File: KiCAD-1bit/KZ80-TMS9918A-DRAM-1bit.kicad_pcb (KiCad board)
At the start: 2 copper layers, 100 x 75 mm, 48 parts, among them J2 EXT_JP, J3 SBC8080 BUS, J4 AD_JP, J5 AD_JP, Q1 2SC1815, U1 TMS9918A, U10 MB8118-16k-1bit-DRAM, U11 MB8118-16k-1bit-DRAM, U12 MB8118-16k-1bit-DRAM, U2 74HCT32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

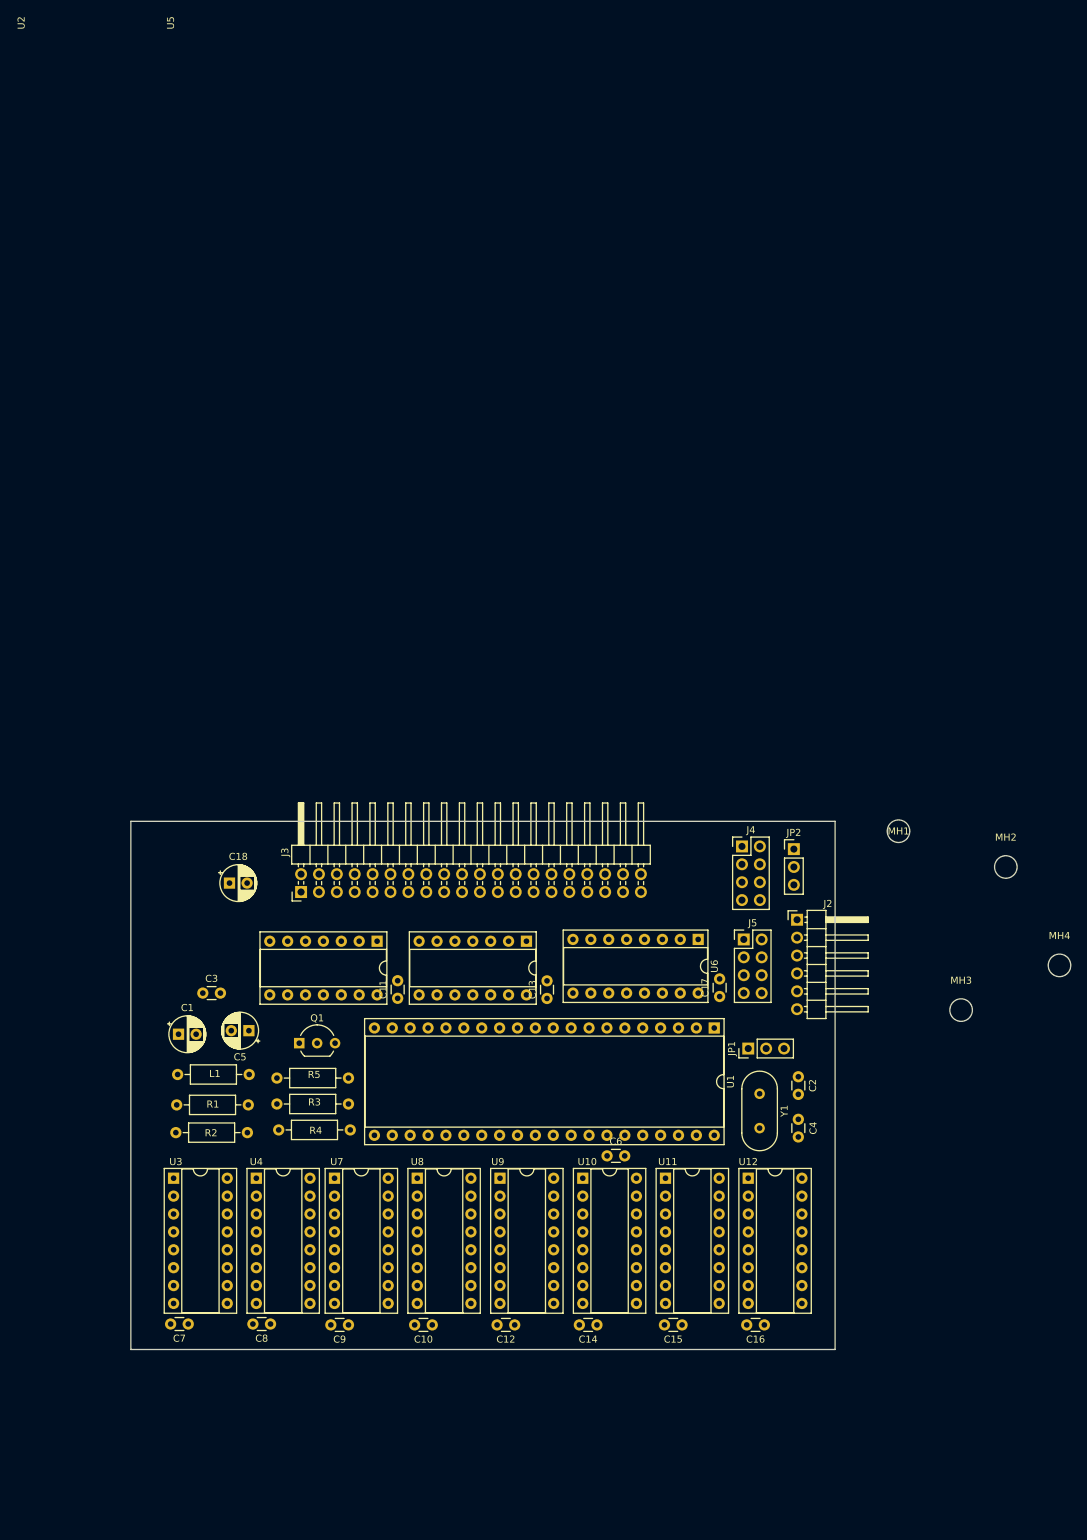
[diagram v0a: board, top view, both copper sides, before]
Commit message: DRAM 16kx1bit版プリントパターン作成
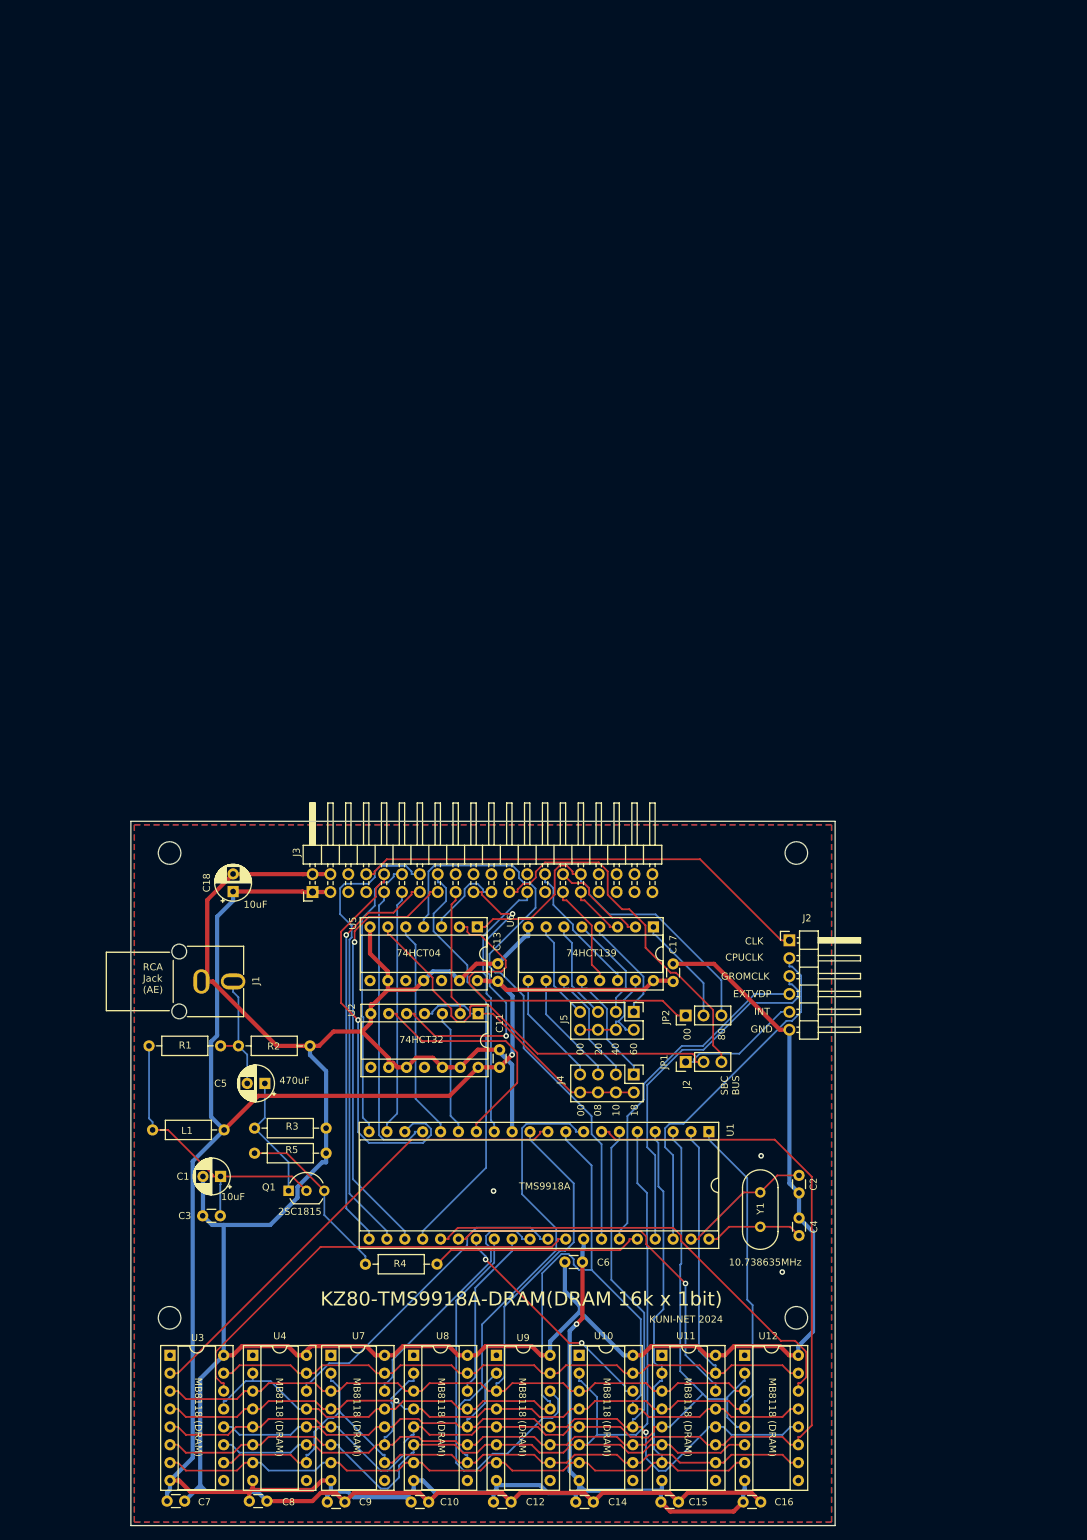
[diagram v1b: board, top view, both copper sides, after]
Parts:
- added J1: Conn_Coaxial, RCA:RCAConAE, F.Cu at (76.0, 78.7)
- moved MH3 120.6 mm to (71.5, 126.5)
- moved MH1 103.6 mm to (71.5, 60.5)
- moved MH4 62.5 mm to (160.5, 126.5)
- moved J4 35.8 mm to (137.4, 91.9), turned to -90 degrees
- moved C3 31.7 mm to (78.7, 112.0), turned to 180 degrees
- moved MH2 29.8 mm to (160.5, 60.5)
- moved R4 29.5 mm to (109.5, 118.9), turned to 180 degrees
- moved JP2 28.2 mm to (144.8, 83.6), turned to 90 degrees
- moved C10 25.2 mm to (108.3, 152.7)
- moved C14 25.2 mm to (131.7, 152.7)
- moved C12 25.2 mm to (120.0, 152.7)
- moved C15 25.2 mm to (143.8, 152.7)
- moved C16 25.2 mm to (155.4, 152.7)
- moved C9 25.2 mm to (96.4, 152.7)
- moved C7 25.2 mm to (73.6, 152.5)
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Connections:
- net Net-(U1-R/~{W}) renamed /R~{W}
- U1 pad 6: /AD1 -> /AD4
- U10 pad 12: /AD1 -> /AD4
- U11 pad 12: /AD1 -> /AD4
- U12 pad 12: /AD1 -> /AD4
- U3 pad 12: unconnected-(U3-A3-Pad12) -> /AD4
- U4 pad 12: /AD1 -> /AD4
- U7 pad 12: /AD1 -> /AD4
- U8 pad 12: /AD1 -> /AD4
- U9 pad 12: /AD1 -> /AD4
- U9 pad 2: /AD1 -> /AD4
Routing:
- net GND: track 0.00 -> 484.4 mm, vias 0 -> 3
- net VCC: track 0.00 -> 333.1 mm, vias 0 -> 2
- net /AD3: track 0.00 -> 172.4 mm
- net /AD2: track 0.00 -> 167.9 mm
- net /AD5: track 0.00 -> 157.1 mm
- net /AD1: track 0.00 -> 153.4 mm
- net /AD4: track 0.00 -> 149.4 mm, vias 0 -> 1
- net /AD7: track 0.00 -> 143.3 mm
- net /AD6: track 0.00 -> 138.3 mm
- net /R~{W}: track 0.00 -> 132.7 mm
- net /~{RAS}: track 0.00 -> 130.7 mm, vias 0 -> 1
- net /~{CAS}: track 0.00 -> 124.0 mm
- net /~{RES}: track 0.00 -> 85.0 mm
- net /AD0: track 0.00 -> 68.0 mm
- net /VD7: track 0.00 -> 66.7 mm
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- added copper zone on B.Cu, net GND
- added copper zone on F.Cu, net GND
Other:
- board size 100 x 75 mm -> 100 x 100 mm
- board text added: "00"
- board text added: "08"
- board text added: "10"
- board text added: "10.738635MHz"
- board text added: "10uF"
- board text added: "18"
- board text added: "20"
- board text added: "2SC1815"
- board text added: "40"
- board text added: "470uF"
- board text added: "60"
- board text added: "74HCT04"
- board text added: "74HCT139"
- board text added: "74HCT32"
- board text added: "80"
- board text added: "CLK"
- board text added: "CPUCLK"
- board text added: "EXTVDP"
- board text added: "GND"
- board text added: "GROMCLK"
- board text added: "INT"
- board text added: "J2"
- board text added: "KUNI-NET 2024"
- board text added: "KZ80-TMS9918A-DRAM(DRAM 16k x 1bit)"
- board text added: "MB8118 (DRAM)"
- board text added: "RCA Jack (AE)"
- board text added: "SBC BUS"
- board text added: "TMS9918A"

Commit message: シルク印刷間違い修正(64bit、16kbit両方) REV1.1ガーバー出力
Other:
- board text added: "REV.1.1"
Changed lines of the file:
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@@
     (aux_axis_origin 66 156)
     (pcbplotparams
-      (layerselection 0x00010fc_ffffffff)
+      (layerselection 0x00010f0_ffffffff)
       (plot_on_all_layers_selection 0x0000000_00000000)
       (disableapertmacros false)
@@
   (gr_rect (start 66 56) (end 166 156)
     (stroke (width 0.1) (type default)) (fill none) (layer "Edge.Cuts"))
-  (gr_text "80" (at 150.5 87.1 90) (layer "F.SilkS")
+  (gr_text "80" (at 145.1 87.1 90) (layer "F.SilkS")
     (effects (font (size 1 1) (thickness 0.15)) (justify left bottom))
   )
@@
     (effects (font (size 1 1) (thickness 0.15)) (justify left bottom))
   )
-  (gr_text "08" (at 132.9 97.9 90) (layer "F.SilkS")
+  (gr_text "08" (at 135.5 98.1 90) (layer "F.SilkS")
     (effects (font (size 1 1) (thickness 0.15)) (justify left bottom))
   )
-  (gr_text "10" (at 135.5 97.9 90) (layer "F.SilkS")
+  (gr_text "10" (at 133 98.1 90) (layer "F.SilkS")
     (effects (font (size 1 1) (thickness 0.15)) (justify left bottom))
   )
@@
     (effects (font (size 1 1) (thickness 0.15)) (justify left bottom))
   )
-  (gr_text "20" (at 133 89.2 90) (layer "F.SilkS")
+  (gr_text "20" (at 135.5 89.2 90) (layer "F.SilkS")
     (effects (font (size 1 1) (thickness 0.15)) (justify left bottom))
   )
@@
     (effects (font (size 1 1) (thickness 0.15)) (justify left bottom))
   )
-  (gr_text "00" (at 145.6 87.1 90) (layer "F.SilkS")
+  (gr_text "00" (at 150.9 87.1 90) (layer "F.SilkS")
     (effects (font (size 1 1) (thickness 0.15)) (justify left bottom))
   )
-  (gr_text "KZ80-TMS9918A-DRAM(DRAM 16k x 1bit)" (at 92.9 125) (layer "F.SilkS")
+  (gr_text "KZ80-TMS9918A-DRAM(DRAM 16k x 1bit)" (at 83.1 125) (layer "F.SilkS")
     (effects (font (size 2 2) (thickness 0.15)) (justify left bottom))
   )
@@
     (effects (font (size 1 1) (thickness 0.15)) (justify left bottom))
   )
-  (gr_text "60" (at 138 89.2 90) (layer "F.SilkS")
+  (gr_text "60" (at 130.5 89.2 90) (layer "F.SilkS")
     (effects (font (size 1 1) (thickness 0.15)) (justify left bottom))
   )
+  (gr_text "REV.1.1" (at 148.5 125.1) (layer "F.SilkS")
+    (effects (font (size 2 2) (thickness 0.15)) (justify left bottom))
+  )
   (gr_text "10uF" (at 82 68.4) (layer "F.SilkS")
     (effects (font (size 1 1) (thickness 0.15)) (justify left bottom))
@@
     (effects (font (size 1 1) (thickness 0.15)) (justify left bottom))
   )
-  (gr_text "18" (at 138.1 97.9 90) (layer "F.SilkS")
+  (gr_text "18" (at 130.2 98.1 90) (layer "F.SilkS")
     (effects (font (size 1 1) (thickness 0.15)) (justify left bottom))
   )
@@
     (effects (font (size 1 1) (thickness 0.15)) (justify left bottom))
   )
-  (gr_text "00" (at 130.5 97.9 90) (layer "F.SilkS")
+  (gr_text "00" (at 138 98 90) (layer "F.SilkS")
     (effects (font (size 1 1) (thickness 0.15)) (justify left bottom))
   )
@@
     (effects (font (size 1 1) (thickness 0.15)) (justify left bottom))
   )
-  (gr_text "00" (at 130.4 89.2 90) (layer "F.SilkS")
+  (gr_text "00" (at 138 89.2 90) (layer "F.SilkS")
     (effects (font (size 1 1) (thickness 0.15)) (justify left bottom))
   )
@@
     (effects (font (size 1 1) (thickness 0.15)) (justify left bottom))
   )
-  (gr_text "40" (at 135.4 89.2 90) (layer "F.SilkS")
+  (gr_text "40" (at 133 89.2 90) (layer "F.SilkS")
     (effects (font (size 1 1) (thickness 0.15)) (justify left bottom))
   )

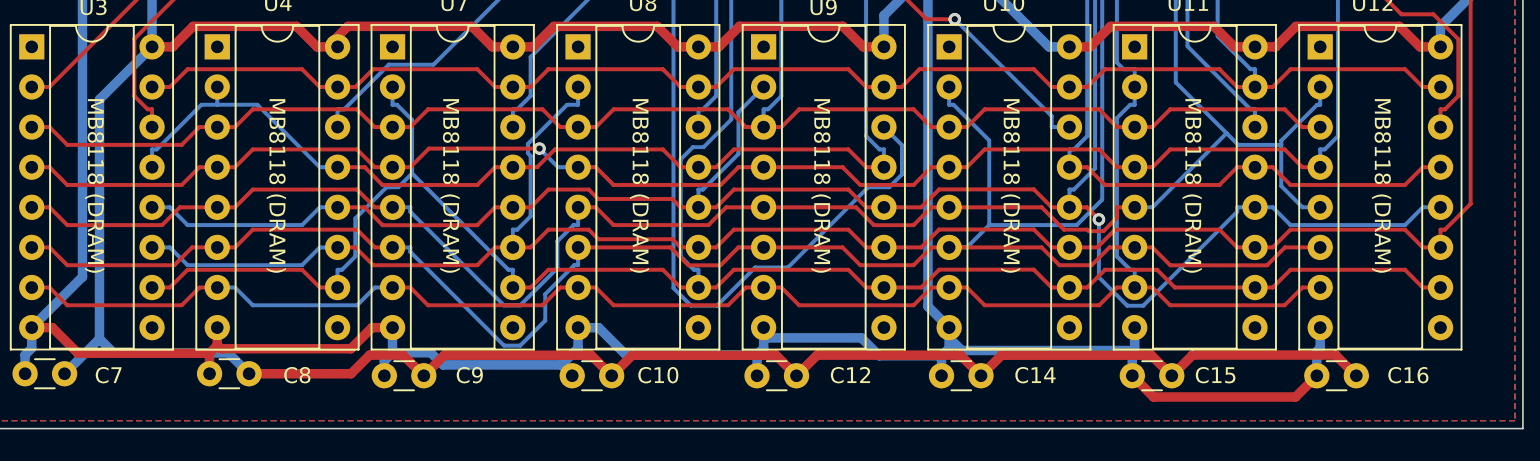
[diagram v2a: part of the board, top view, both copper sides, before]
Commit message: 64k版 部品配置調整、16k版 4164 DRAM対応版 ガーバーデータ出力
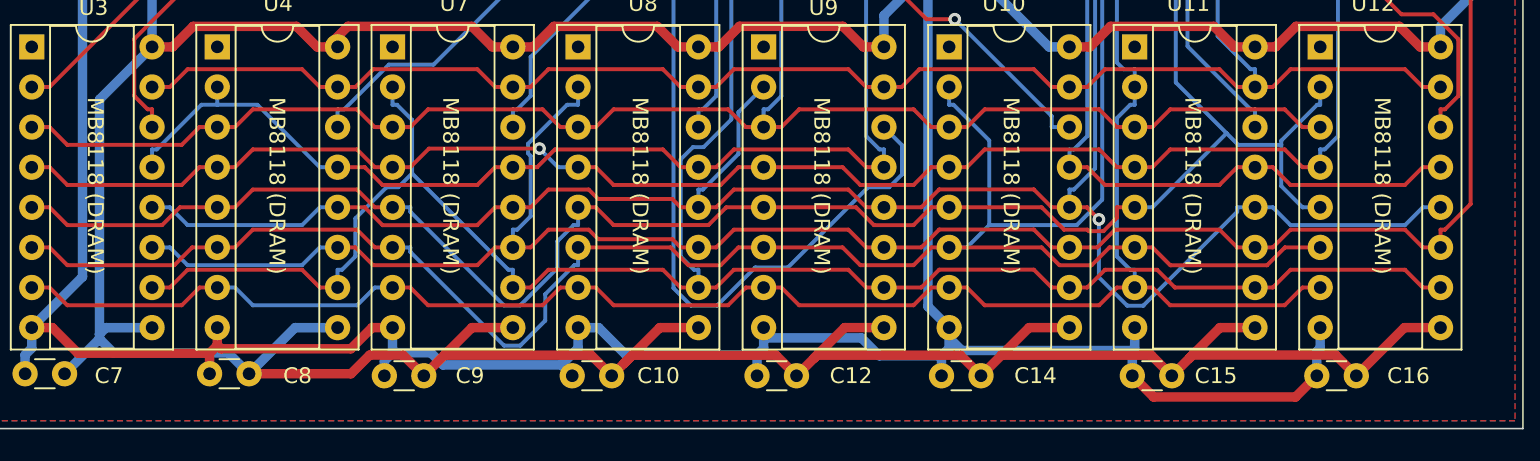
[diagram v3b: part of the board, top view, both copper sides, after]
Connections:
- U10 pad 9: unconnected-(U10-NC-Pad9) -> GND
- U11 pad 9: unconnected-(U11-NC-Pad9) -> GND
- U12 pad 9: unconnected-(U12-NC-Pad9) -> GND
- U3 pad 9: unconnected-(U3-NC-Pad9) -> GND
- U4 pad 9: unconnected-(U4-NC-Pad9) -> GND
- U7 pad 9: unconnected-(U7-NC-Pad9) -> GND
- U8 pad 9: unconnected-(U8-NC-Pad9) -> GND
- U9 pad 9: unconnected-(U9-NC-Pad9) -> GND
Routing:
- net GND: track 484.4 -> 527.2 mm
